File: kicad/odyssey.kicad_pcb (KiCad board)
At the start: 2 copper layers, 27.5 x 26.5 mm, 8 parts, among them J1 MSD-4-A, U1 I3G4250DTR, U2 IIS2MDCTR, U3 XIAO-RP2040-SMD, U4 TL3305AF260QG, U5 MPL3115A2

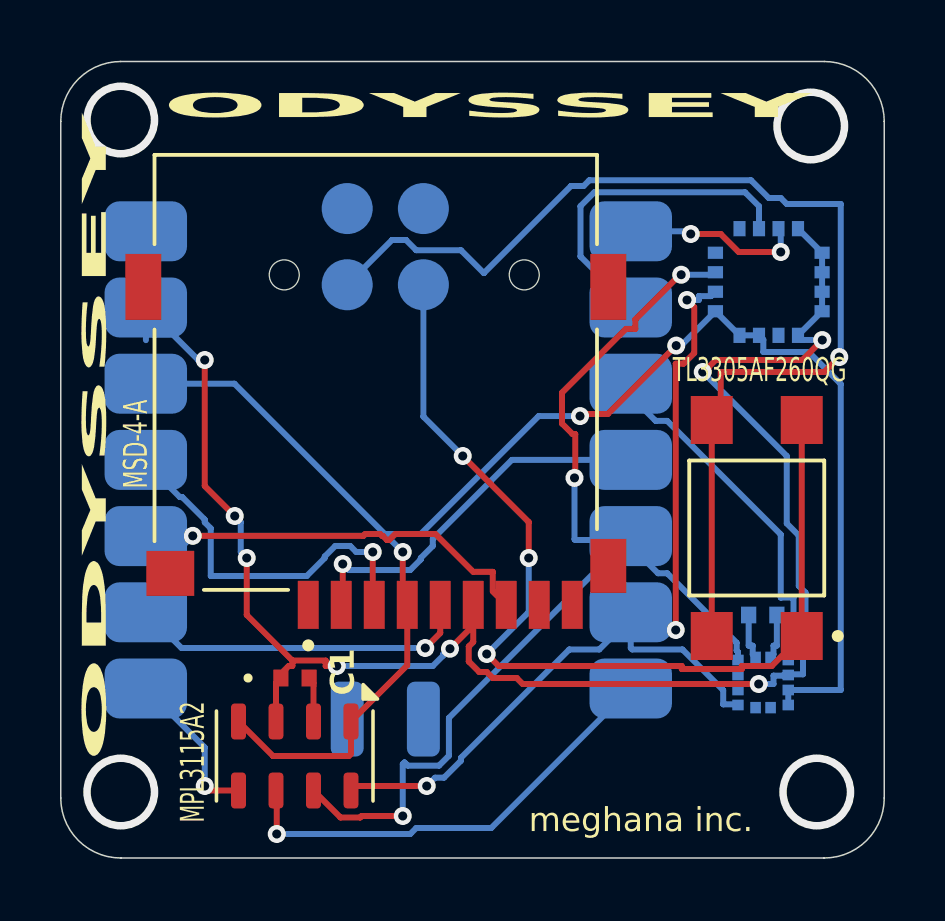
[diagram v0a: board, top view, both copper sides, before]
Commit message: feat: shrink board and autoroute
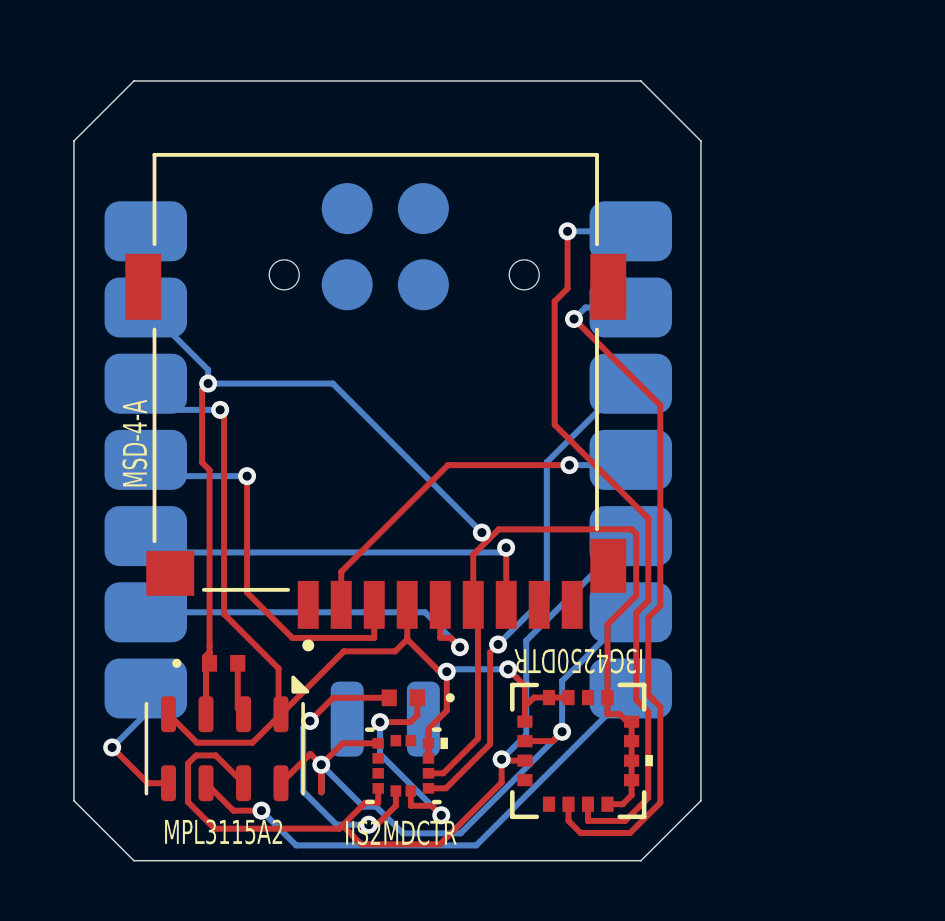
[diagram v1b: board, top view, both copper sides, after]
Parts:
- removed U4: TL3305AF260QG, footprints:SW_TL3305AF260QG
- C3, U1, U2: moved to F.Cu
- moved U1 16.9 mm to (71.2, 66.0)
- moved U2 12.3 mm to (65.4, 66.5)
- moved C3 12.3 mm to (65.4, 64.3)
- moved C1 2.43 mm to (59.4, 63.1)
- moved U5 2.35 mm to (59.5, 66.0)
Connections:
- U3 pad 19: Net-(U3-RST) -> unconnected-(U3-RST-Pad19)
- U3 pad 20: Net-(U3-GND-Pad20) -> unconnected-(U3-GND-Pad20)
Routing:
- net Net-(U3-GND-Pad20): track 37.3 -> 0.00 mm, vias 1 -> 0
- net Net-(U3-RST): track 33.0 -> 0.00 mm, vias 3 -> 0
- net I3G4 INT1: track 6.09 -> 25.7 mm, vias 2 -> 1
- net 3.3V XIAO: track 54.7 -> 35.3 mm
- net I3G4 INT2: track 11.2 -> 24.1 mm, vias 0 -> 1
- net Net-(U2-C1): track 1.59 -> 10.6 mm, vias 0 -> 2
- net GND: track 60.1 -> 51.4 mm, vias 8 -> 2
- net XIAO SDA: track 36.5 -> 28.4 mm, vias 3 -> 1
- net XIAO SCL: track 32.2 -> 24.4 mm, vias 3 -> 2
- net Net-(C3-Pad1): track 1.56 -> 8.22 mm, vias 0 -> 2
- net IIS2 INT: track 12.2 -> 16.7 mm, vias 0 -> 1
- net MPL INT1: track 15.3 -> 17.2 mm
- net CLK: track 11.5 -> 12.8 mm
- net MOSI: track 12.5 -> 13.5 mm
- net (no net): vias 4 -> 0
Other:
- board size 27.5 x 26.5 mm -> 20.9 x 26 mm
- board text removed: "C1"
- board text removed: "TL3305AF260QG"

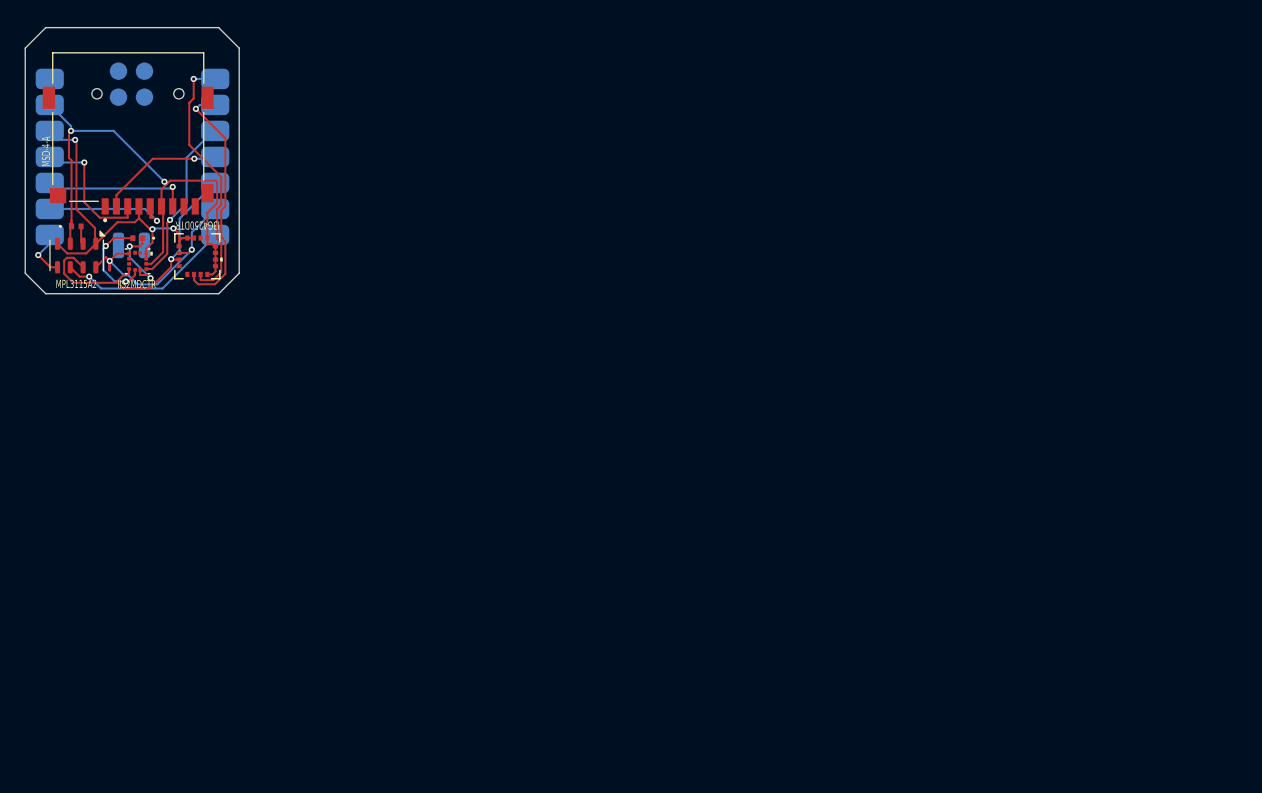
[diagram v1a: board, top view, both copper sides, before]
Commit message: updating pcb
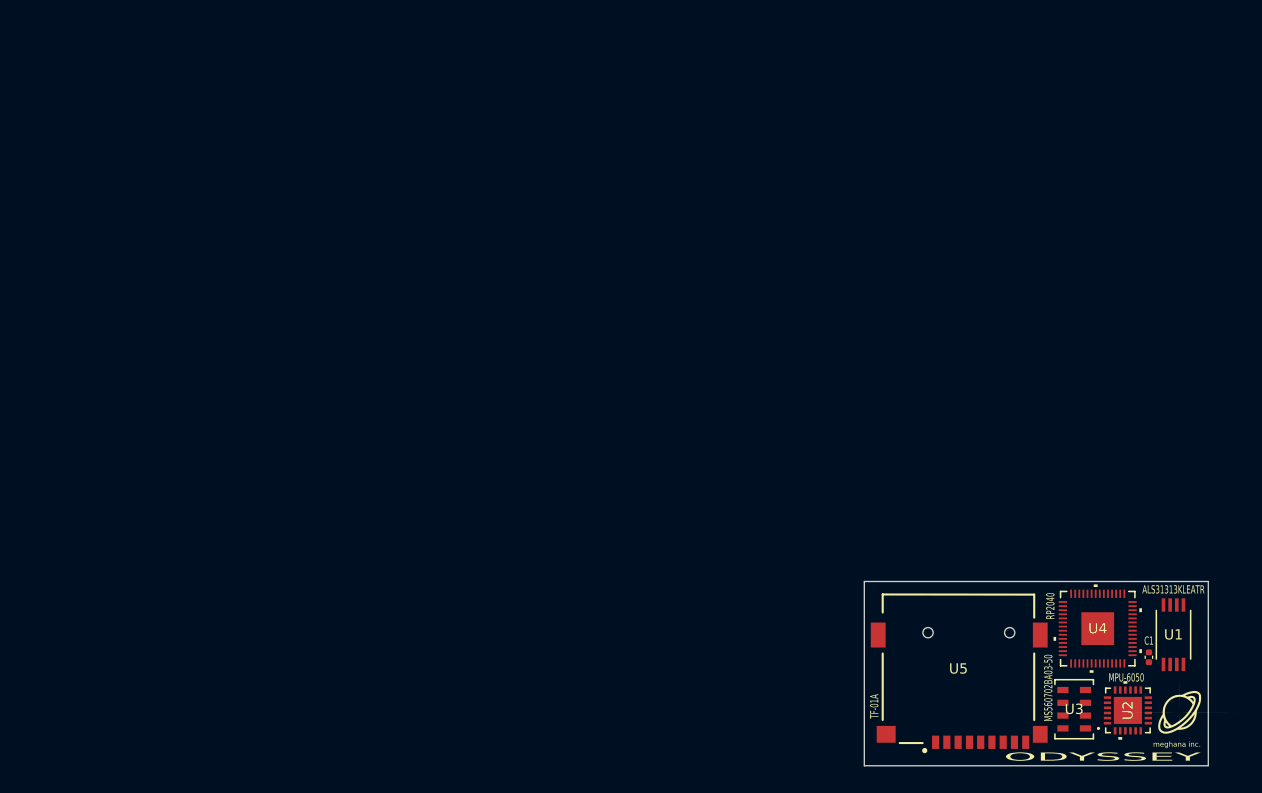
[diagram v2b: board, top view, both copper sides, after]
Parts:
- removed C3: C2, footprints:CAP_0402_N_WAL
- removed J1: MSD-4-A, footprints:CUI_MSD-4-A
- added G***: LOGO, LOGO, F.Cu at (167.2, 110.4)
- added U4: RP2040, footprints:IC57_RP2040, F.Cu at (159.2, 102.4)
- C1: value 0402B104K160CT -> C; footprint footprints:CAP_0402_N_WAL -> Capacitor_SMD:C_0402_1005Metric
- U1: value I3G4250DTR -> ALS31313KLEATR; footprint footprints:I3G4250DTR -> footprints:TSSOP8_LE_ALM
- U2: value IIS2MDCTR -> MPU-6050; footprint footprints:IIS2MDCTR -> footprints:QFN24_4X4X0P9-0P5_TDK
- U3: value XIAO-RP2040-SMD -> MS560702BA03-50; footprint footprints:XIAO-RP2040-SMD -> footprints:SON8_MS5611_TEC; moved to F.Cu
- U5: value MPL3115A2 -> TF-01A; footprint Package_LGA:NXP_LGA-8_3x5mm_P1.25mm_H1.1mm -> footprints:TF-01A
- moved C1 112.9 mm to (164.2, 105.2), turned to -90 degrees
- moved U3 106.6 mm to (156.9, 110.3)
- moved U2 106.2 mm to (162.1, 110.4), turned to 180 degrees
- moved U1 102.3 mm to (166.6, 103.0), turned to 90 degrees
- moved U5 95.1 mm to (145.6, 106.3), turned to 180 degrees
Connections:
- C1 pad 2: Net-(U5-CAP) -> Net-(U2-REGOUT)
- U1 pad 1: 3.3V XIAO -> 3.3V
- U1 pad 2: XIAO SCL -> unconnected-(U1-ADR0-Pad2)
- U1 pad 3: XIAO SDA -> GND
- U1 pad 4: unconnected-(U1-SDO/SA0-Pad4) -> MAGINT
- U1 pad 6: I3G4 INT2 -> unconnected-(U1-ADR1-Pad6)
- U1 pad 7: I3G4 INT1 -> SDA
- U1 pad 8: GND -> SCL
- U2 pad 1: XIAO SCL -> GND
- U2 pad 10: 3.3V XIAO -> Net-(U2-REGOUT)
- U2 pad 11: unconnected-(U2-NC-Pad11) -> GYROFSYNC
- U2 pad 12: unconnected-(U2-NC-Pad12) -> GYROINT
- U2 pad 4: XIAO SDA -> unconnected-(U2-NC-Pad4)
- U2 pad 5: Net-(U2-C1) -> unconnected-(U2-NC-Pad5)
- U2 pad 6: Net-(C3-Pad1) -> unconnected-(U2-AUX_DA-Pad6)
- U2 pad 7: IIS2 INT -> unconnected-(U2-AUX_CL-Pad7)
- U2 pad 8: GND -> 3.3V
- U2 pad 9: 3.3V XIAO -> unconnected-(U2-AD0-Pad9)
- U3 pad 1: I3G4 INT1 -> 3.3V
- U3 pad 2: I3G4 INT2 -> 3.3V
- U3 pad 3: IIS2 INT -> GND
- U3 pad 4: MSD STAT -> unconnected-(U3-CSB-Pad4)
- U3 pad 5: XIAO SDA -> unconnected-(U3-CSB-Pad5)
- U3 pad 6: XIAO SCL -> unconnected-(U3-SDO-Pad6)
- U3 pad 7: MPL INT1 -> SDA
- U3 pad 8: MPL INT2 -> SCL
- U5 pad 1: 3.3V XIAO -> unconnected-(U5-DAT2-Pad1)
- U5 pad 2: Net-(U5-CAP) -> CD
- U5 pad 3: GND -> MSDMOSI
- U5 pad 4: 3.3V XIAO -> 3.3V
- U5 pad 5: MPL INT2 -> MSDCLK
- U5 pad 6: MPL INT1 -> GND
- U5 pad 7: XIAO SDA -> MSDMISO
- U5 pad 8: XIAO SCL -> unconnected-(U5-DAT1-Pad8)
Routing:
- net GND: track 51.4 -> 0.00 mm, vias 2 -> 0
- net 3.3V XIAO: track 35.3 -> 0.00 mm, vias 3 -> 0
- net XIAO SDA: track 28.4 -> 0.00 mm, vias 1 -> 0
- net I3G4 INT1: track 25.7 -> 0.00 mm, vias 1 -> 0
- net XIAO SCL: track 24.4 -> 0.00 mm, vias 2 -> 0
- net I3G4 INT2: track 24.1 -> 0.00 mm, vias 1 -> 0
- net MPL INT1: track 17.2 -> 0.00 mm, vias 1 -> 0
- net IIS2 INT: track 16.7 -> 0.00 mm, vias 1 -> 0
- net MISO: track 14.2 -> 0.00 mm, vias 1 -> 0
- net MOSI: track 13.5 -> 0.00 mm, vias 1 -> 0
- net CLK: track 12.8 -> 0.00 mm, vias 1 -> 0
- net MSD STAT: track 12.3 -> 0.00 mm, vias 1 -> 0
- net Net-(U2-C1): track 10.6 -> 0.00 mm, vias 2 -> 0
- net Net-(C3-Pad1): track 8.22 -> 0.00 mm, vias 2 -> 0
- net MPL INT2: track 4.80 -> 0.00 mm, vias 1 -> 0
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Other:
- board size 20.9 x 26 mm -> 33.6 x 18 mm

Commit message: trying firmware stuff
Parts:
- added C2: C, Capacitor_SMD:C_0402_1005Metric, F.Cu at (163.6, 103.2)
- U1: value ALS31313KLEATR -> ALS31313KLEATR-1000
- U4: value RP2040 -> XIAO-RP2040-SMD; footprint footprints:IC57_RP2040 -> footprints:XIAO-RP2040-SMD; moved to B.Cu
- moved U2 8.56 mm to (159.6, 102.2), turned to -90 degrees
- moved C1 4.64 mm to (163.6, 100.6), turned to 180 degrees
- moved U4 3.88 mm to (158.4, 106.2), turned to 90 degrees
- moved U3 3.43 mm to (160.1, 109.1), turned to -90 degrees
- moved U1 1.80 mm to (166.6, 101.2), turned to -90 degrees
- moved U5 1.40 mm to (147.0, 106.3)
- moved G*** 1.00 mm to (167.8, 111.2)
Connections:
- U1 pad 2: unconnected-(U1-ADR0-Pad2) -> GND
- U1 pad 6: unconnected-(U1-ADR1-Pad6) -> GND
- U2 pad 20: unconnected-(U2-CPOUT-Pad20) -> Net-(U2-CPOUT)
- U2 pad 9: unconnected-(U2-AD0-Pad9) -> GND
- U3 pad 6: unconnected-(U3-SDO-Pad6) -> GND
- U4 pad 1: Net-(U4-IOVDD-Pad1) -> MAGINT
- U4 pad 10: Net-(U4-IOVDD-Pad1) -> MSDMISO
- U4 pad 11: unconnected-(U4-GPIO8-Pad11) -> MSDMOSI
- U4 pad 12: unconnected-(U4-GPIO9-Pad12) -> 3.3V
- U4 pad 13: unconnected-(U4-GPIO10-Pad13) -> GND
- U4 pad 16: MSDCLK -> unconnected-(U4-GND-Pad16)
- U4 pad 17: MSDMISO -> unconnected-(U4-SWDIO-Pad17)
- U4 pad 18: MSDMOSI -> unconnected-(U4-SWDCLK-Pad18)
- U4 pad 2: SDA -> GYROINT
- U4 pad 3: SCL -> GYROFSYNC
- U4 pad 4: MAGINT -> MSDCD
- U4 pad 5: GYROINT -> SDA
- U4 pad 6: GYROFSYNC -> SCL
- U4 pad 7: CD -> unconnected-(U4-GPIO0_D6_TX-Pad7)
- U4 pad 9: unconnected-(U4-GPIO7-Pad9) -> MSDCLK
- U5 pad 2: CD -> MSDCD
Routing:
- net GND: track 0.00 -> 106.5 mm, vias 0 -> 3
- net 3.3V: track 0.00 -> 50.5 mm, vias 0 -> 3
- net SCL: track 0.00 -> 35.5 mm, vias 0 -> 2
- net MSDMISO: track 0.00 -> 28.0 mm, vias 0 -> 1
- net Net-(U2-REGOUT): track 0.00 -> 26.2 mm, vias 0 -> 2
- net SDA: track 0.00 -> 24.0 mm, vias 0 -> 1
- net MSDMOSI: track 0.00 -> 20.6 mm, vias 0 -> 1
- net MSDCD: track 0.00 -> 19.9 mm, vias 0 -> 1
- net MAGINT: track 0.00 -> 18.8 mm, vias 0 -> 1
- net MSDCLK: track 0.00 -> 17.3 mm, vias 0 -> 1
- net GYROFSYNC: track 0.00 -> 14.0 mm, vias 0 -> 1
- net GYROINT: track 0.00 -> 13.2 mm, vias 0 -> 1
- net Net-(U2-CPOUT): track 0.00 -> 1.58 mm
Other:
- board size 33.6 x 18 mm -> 32.8 x 20.8 mm
